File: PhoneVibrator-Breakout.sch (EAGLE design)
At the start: 2 parts

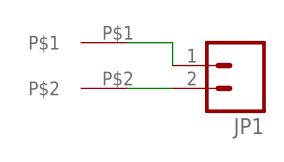
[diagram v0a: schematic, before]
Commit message: Fixed issue with where I placed the mechanical pad
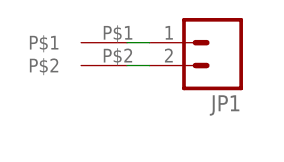
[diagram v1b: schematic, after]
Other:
- moved on the sheet: JP1
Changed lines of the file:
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@@
 <instances>
 <instance part="U$1" gate="G$1" x="7.62" y="5.08" rot="R270"/>
-<instance part="JP1" gate="G$1" x="20.32" y="5.08" rot="R180"/>
+<instance part="JP1" gate="G$1" x="17.78" y="7.62" rot="R180"/>
 </instances>
 <busses>
@@
 <pinref part="U$1" gate="G$1" pin="P$1"/>
 <pinref part="JP1" gate="G$1" pin="1"/>
-<wire x1="7.62" y1="7.62" x2="12.7" y2="7.62" width="0.1524" layer="91"/>
-<wire x1="12.7" y1="7.62" x2="12.7" y2="5.08" width="0.1524" layer="91"/>
+<wire x1="7.62" y1="7.62" x2="10.16" y2="7.62" width="0.1524" layer="91"/>
 </segment>
 </net>
@@
 <pinref part="U$1" gate="G$1" pin="P$2"/>
 <pinref part="JP1" gate="G$1" pin="2"/>
-<wire x1="7.62" y1="2.54" x2="12.7" y2="2.54" width="0.1524" layer="91"/>
+<wire x1="7.62" y1="5.08" x2="10.16" y2="5.08" width="0.1524" layer="91"/>
 </segment>
 </net>
